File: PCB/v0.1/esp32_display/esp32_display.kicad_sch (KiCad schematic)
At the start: 6 parts, among them J1 USB_B_Micro

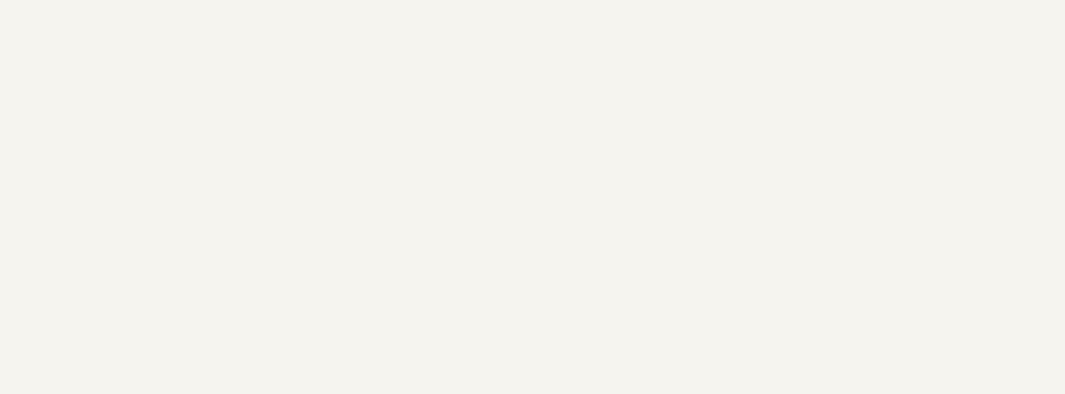
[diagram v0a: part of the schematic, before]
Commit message: Add housing edge, generate output files
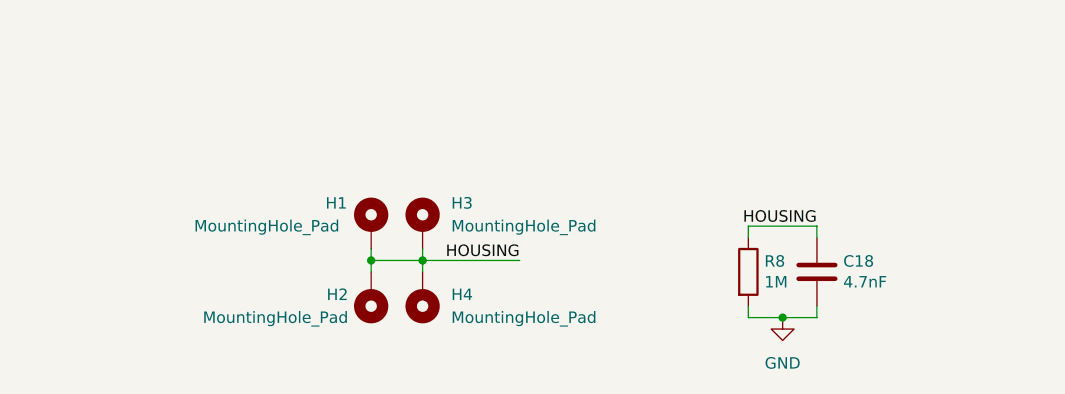
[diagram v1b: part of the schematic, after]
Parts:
- added C18: 4.7nF, Capacitor_SMD:C_0603_1608Metric_Pad1.08x0.95mm_HandSolder, symbol Device:C
- added H1, H2, H3, H4: MountingHole_Pad, MountingHole:MountingHole_2.2mm_M2_Pad_Via, symbol Mechanical:MountingHole_Pad
- added R8: 1M, Resistor_SMD:R_0603_1608Metric_Pad0.98x0.95mm_HandSolder, symbol Device:R
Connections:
- net GND: now also C18.2, R8.2
- new net HOUSING: C18.1, H1.1, H2.1, H3.1, H4.1, R8.1

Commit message: Smaller footprint, no housing, right angle buttons
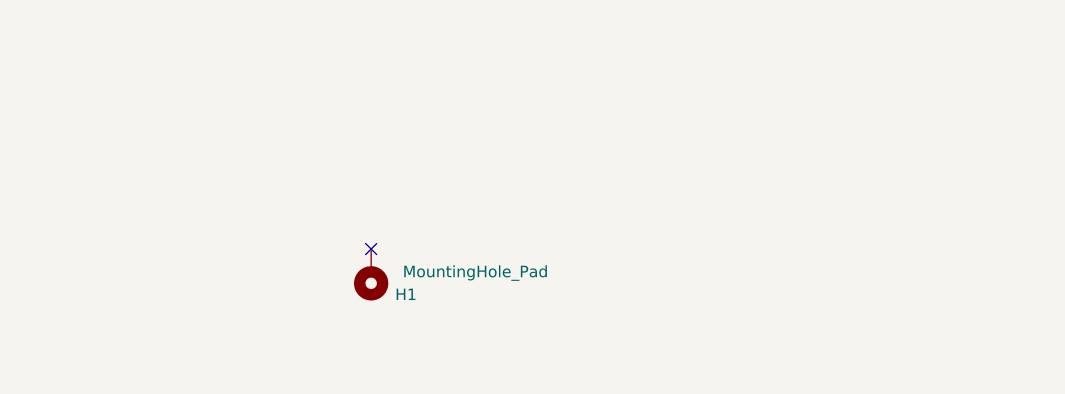
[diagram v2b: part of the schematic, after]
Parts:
- removed C18: 4.7nF, Capacitor_SMD:C_0603_1608Metric_Pad1.08x0.95mm_HandSolder, symbol Device:C
- removed H2, H3, H4: MountingHole_Pad, MountingHole:MountingHole_2.2mm_M2_Pad_Via, symbol Mechanical:MountingHole_Pad
- removed R8: 1M, Resistor_SMD:R_0603_1608Metric_Pad0.98x0.95mm_HandSolder, symbol Device:R
- H1: footprint MountingHole:MountingHole_2.2mm_M2_Pad_Via -> MountingHole:MountingHole_3.2mm_M3_ISO14580
- J1: footprint Connector_USB:USB_Micro-B_Amphenol_10118194_Horizontal -> Connector_USB:USB_Micro-B_Molex-105017-0001
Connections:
- net HOUSING: no longer names the net of H1.1
- no-connect marks 3 -> 4
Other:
- moved on the sheet: H1

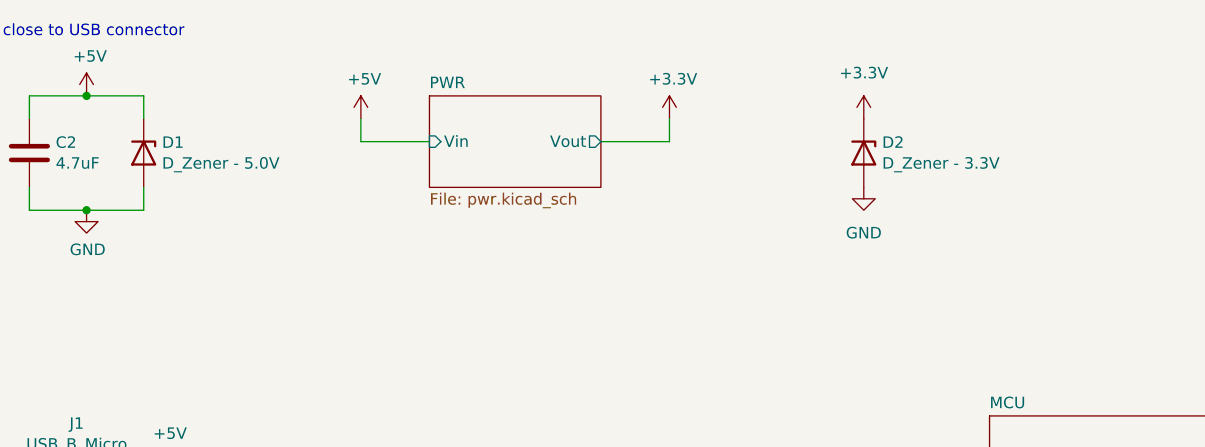
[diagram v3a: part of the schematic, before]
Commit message: Rename TVS/ESD protection diodes to their name (5V and 3.3V)
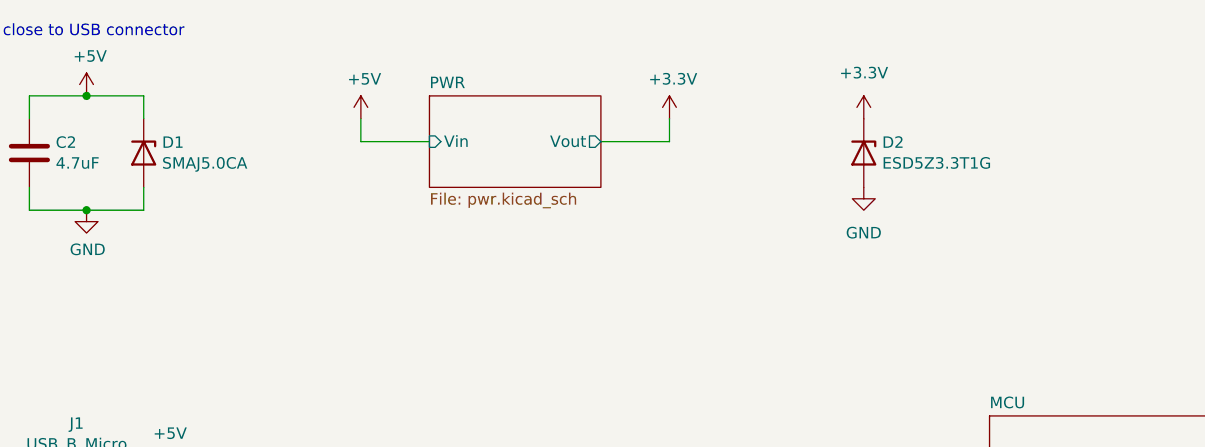
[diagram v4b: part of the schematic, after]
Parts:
- D1: value D_Zener - 5.0V -> SMAJ5.0CA
- D2: value D_Zener - 3.3V -> ESD5Z3.3T1G
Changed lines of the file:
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@@
       (effects (font (size 1.27 1.27)) (justify left))
     )
-    (property "Value" "D_Zener - 5.0V" (id 1) (at 42.672 30.353 90)
+    (property "Value" "SMAJ5.0CA" (id 1) (at 42.672 30.353 90)
       (effects (font (size 1.27 1.27)) (justify left))
     )
@@
       (effects (font (size 1.27 1.27)) (justify left))
     )
-    (property "Value" "D_Zener - 3.3V" (id 1) (at 122.682 30.353 90)
+    (property "Value" "ESD5Z3.3T1G" (id 1) (at 122.682 30.353 90)
       (effects (font (size 1.27 1.27)) (justify left))
     )
@@
     )
     (path "/00000000-0000-0000-0000-000061d468d4"
-      (reference "D1") (unit 1) (value "D_Zener - 5.0V") (footprint "Diode_SMD:D_SMA")
+      (reference "D1") (unit 1) (value "SMAJ5.0CA") (footprint "Diode_SMD:D_SMA")
     )
     (path "/628a4757-ac1e-4171-94bc-10225db0e9cd"
-      (reference "D2") (unit 1) (value "D_Zener - 3.3V") (footprint "Diode_SMD:D_SOD-523")
+      (reference "D2") (unit 1) (value "ESD5Z3.3T1G") (footprint "Diode_SMD:D_SOD-523")
     )
     (path "/00000000-0000-0000-0000-000061c723b1/3bdaab53-16cc-4327-8283-60d1698101e7"

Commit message: Fix 3d models, generate outputs, add .wrl to outputs
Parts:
- J1: footprint Connector_USB:USB_Micro-B_Molex-105017-0001 -> myLib:USB_Micro-B_Molex-105017-0001
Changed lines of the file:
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@@
     (property "Reference" "J1" (id 0) (at 33.1978 59.2582 0))
     (property "Value" "USB_B_Micro" (id 1) (at 33.1978 61.5696 0))
-    (property "Footprint" "Connector_USB:USB_Micro-B_Molex-105017-0001" (id 2) (at 35.56 72.39 0)
+    (property "Footprint" "myLib:USB_Micro-B_Molex-105017-0001" (id 2) (at 35.56 72.39 0)
       (effects (font (size 1.27 1.27)) hide)
     )
@@
     )
     (path "/00000000-0000-0000-0000-000061c015be"
-      (reference "J1") (unit 1) (value "USB_B_Micro") (footprint "Connector_USB:USB_Micro-B_Molex-105017-0001")
+      (reference "J1") (unit 1) (value "USB_B_Micro") (footprint "myLib:USB_Micro-B_Molex-105017-0001")
     )
     (path "/00000000-0000-0000-0000-000061c723b1/785bf931-de50-44b9-a6a1-eebb5527f4a4"
